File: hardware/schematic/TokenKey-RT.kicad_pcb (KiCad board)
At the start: 4 copper layers, 50 x 40 mm, 103 parts, among them J1 USB-C, J2 Header 1x04 P2.54 H3.0 (OLED), J3 TC2030-NL, Q1 AO3401A, SW1 SW_BOOT, SW2 EC11E18244A5, SW3 BTN1, SW4 BTN2, U1 MIMXRT1062DVL6B, U2 AP2112K-3.3TRG1, U3 TLV62569DBVR, U4 W25Q64JVSSIQ, U5 APS6404L-3SQR-ZR, U6 USBLC6-2SC6, Y1 24MHz 12pF, Y2 32.768kHz 12.5pF

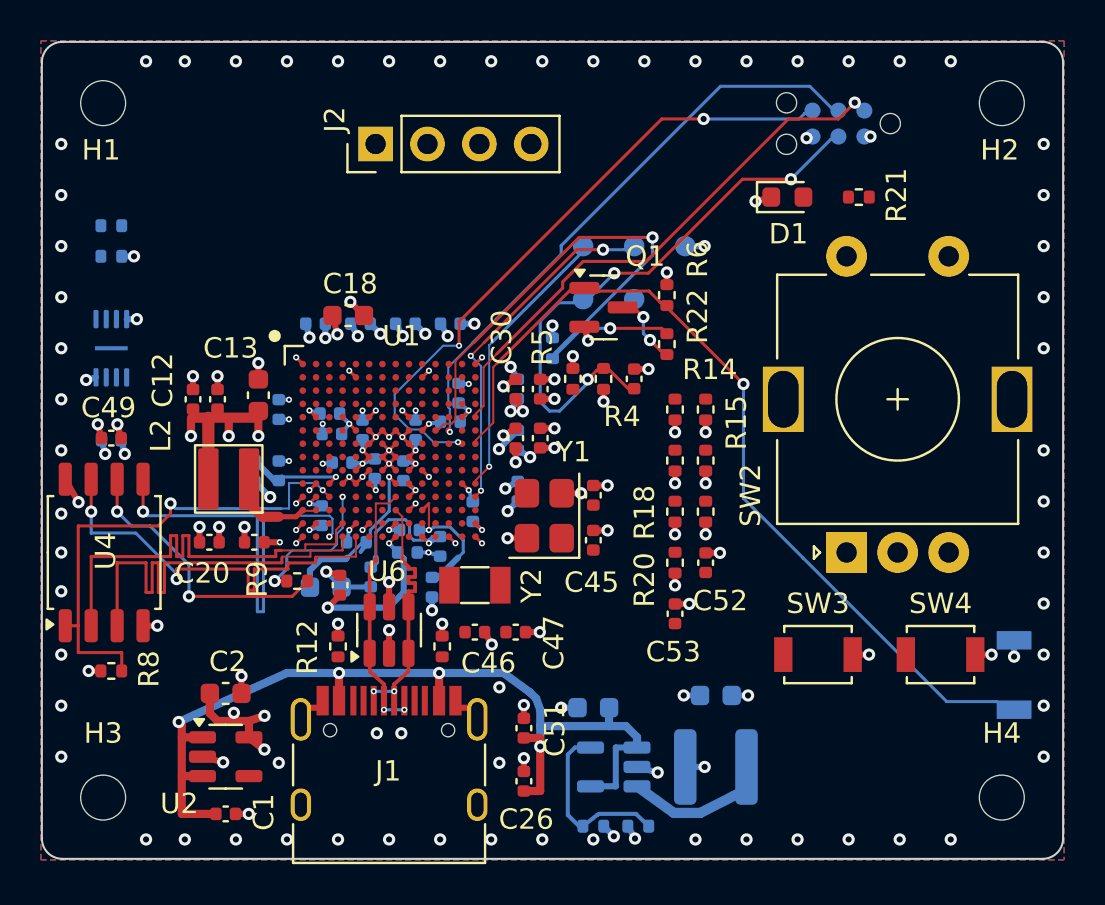
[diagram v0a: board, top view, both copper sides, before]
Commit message: Group B non-U1 legs: R14/R15-J2, D1-R21, R16-C52-SW2, C53-R17-SW2, R18-SW2, R19-SW3, R20-SW4
Part of #60
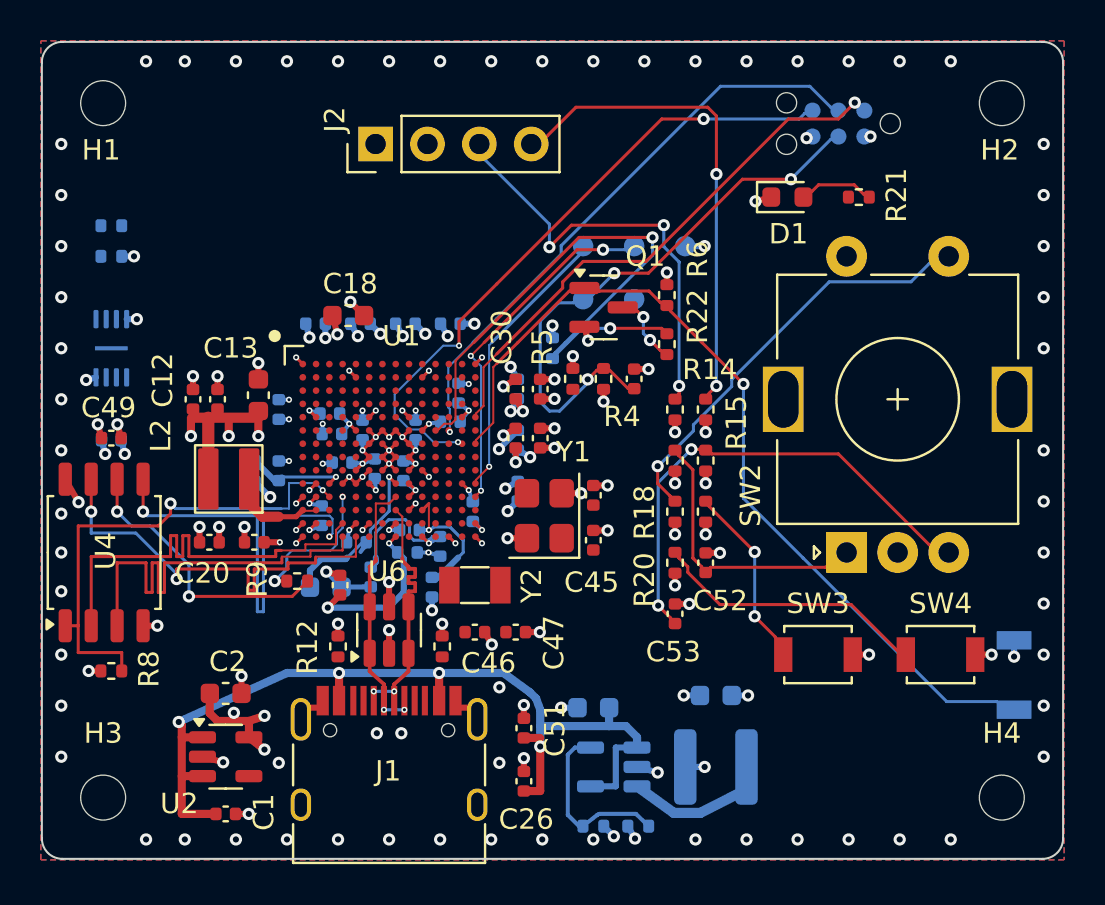
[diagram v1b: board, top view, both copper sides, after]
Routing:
- net ENC_B: track 0.00 -> 24.1 mm, vias 0 -> 2
- net OLED_SDA: track 0.00 -> 24.0 mm, vias 0 -> 2
- net OLED_SCL: track 0.00 -> 21.3 mm, vias 0 -> 3
- net ENC_SW: track 0.00 -> 20.9 mm, vias 0 -> 1
- net ENC_A: track 0.00 -> 13.8 mm
- net BTN2: track 0.00 -> 13.5 mm
- net BTN1: track 0.00 -> 8.99 mm, vias 0 -> 2
- net LED_A: track 0.00 -> 3.66 mm

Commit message: Route CC2 (J1 B5-R13) and 24 MHz XTALI/XTALO U1-Y1, Y1-C44 (no vias; guard ring pending)
Part of #60
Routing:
- net XTALI: track 0.00 -> 9.21 mm
- net XTALO: track 0.00 -> 6.26 mm
- net CC2: track 0.00 -> 2.60 mm
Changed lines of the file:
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@@
 	)
 	(segment
+		(start 18.825 30.625)
+		(end 19.275 30.175)
+		(width 0.15)
+		(layer "F.Cu")
+		(net 3)
+	)
+	(segment
+		(start 18.75 32.255)
+		(end 18.825 31.525)
+		(width 0.15)
+		(layer "F.Cu")
+		(net 3)
+	)
+	(segment
+		(start 19.275 30.175)
+		(end 19.6 30.11)
+		(width 0.15)
+		(layer "F.Cu")
+		(net 3)
+	)
+	(segment
+		(start 18.825 31.525)
+		(end 18.825 30.625)
+		(width 0.15)
+		(layer "F.Cu")
+		(net 3)
+	)
+	(segment
 		(start 30.775 13.175)
 		(end 32.325 14.725)
@@
 	)
 	(segment
+		(start 22.275 25.275)
+		(end 24.3 25.275)
+		(width 0.15)
+		(layer "F.Cu")
+		(net 16)
+	)
+	(segment
+		(start 25.975 23.65)
+		(end 26.725 22.9)
+		(width 0.15)
+		(layer "F.Cu")
+		(net 16)
+	)
+	(segment
+		(start 20.45 25.275)
+		(end 22.275 25.275)
+		(width 0.1)
+		(layer "F.Cu")
+		(net 16)
+	)
+	(segment
+		(start 24.3 25.275)
+		(end 24.85 24.725)
+		(width 0.15)
+		(layer "F.Cu")
+		(net 16)
+	)
+	(segment
+		(start 19.425 24.25)
+		(end 20.45 25.275)
+		(width 0.1)
+		(layer "F.Cu")
+		(net 16)
+	)
+	(segment
+		(start 26.725 22.9)
+		(end 27 22.68)
+		(width 0.15)
+		(layer "F.Cu")
+		(net 16)
+	)
+	(segment
+		(start 25.45 24.3)
+		(end 25.975 23.65)
+		(width 0.15)
+		(layer "F.Cu")
+		(net 16)
+	)
+	(segment
+		(start 24.85 24.725)
+		(end 25.45 24.3)
+		(width 0.15)
+		(layer "F.Cu")
+		(net 16)
+	)
+	(segment
+		(start 19.275 24.225)
+		(end 19.425 24.25)
+		(width 0.1)
+		(layer "F.Cu")
+		(net 16)
+	)
+	(segment
 		(start 18.625 24.225)
 		(end 18.95 24.55)
@@
 	)
 	(segment
+		(start 21.35 23.25)
+		(end 22.2 22.4)
+		(width 0.1)
+		(layer "F.Cu")
+		(net 39)
+	)
+	(segment
+		(start 22.9 21.275)
+		(end 23.175 21.55)
+		(width 0.15)
+		(layer "F.Cu")
+		(net 39)
+	)
+	(segment
+		(start 19.425 23.525)
+		(end 19.7 23.25)
+		(width 0.1)
+		(layer "F.Cu")
+		(net 39)
+	)
+	(segment
+		(start 22.2 22.4)
+		(end 22.2 21.525)
+		(width 0.1)
+		(layer "F.Cu")
+		(net 39)
+	)
+	(segment
+		(start 23.175 21.55)
+		(end 23.75 22.1)
+		(width 0.15)
+		(layer "F.Cu")
+		(net 39)
+	)
+	(segment
+		(start 22.275 21.45)
+		(end 22.45 21.275)
+		(width 0.15)
+		(layer "F.Cu")
+		(net 39)
+	)
+	(segment
+		(start 22.2 21.525)
+		(end 22.275 21.45)
+		(width 0.1)
+		(layer "F.Cu")
+		(net 39)
+	)
+	(segment
+		(start 19.275 23.575)
+		(end 19.425 23.525)
+		(width 0.1)
+		(layer "F.Cu")
+		(net 39)
+	)
+	(segment
+		(start 19.7 23.25)
+		(end 21.35 23.25)
+		(width 0.1)
+		(layer "F.Cu")
+		(net 39)
+	)
+	(segment
+		(start 22.45 21.275)
+		(end 22.9 21.275)
+		(width 0.15)
+		(layer "F.Cu")
+		(net 39)
+	)
+	(segment

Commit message: Route CC1 (J1 A5-R12) with J1 pad-pitch-limited breakout DRU exception (CC1 in J1 courtyard, 0.15 mm)
Part of #60
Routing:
- net CC1: track 0.00 -> 2.76 mm
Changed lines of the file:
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@@
+	)
+	(segment
+		(start 15.75 31.2)
+		(end 14.66 30.11)
+		(width 0.15)
+		(layer "F.Cu")
+		(net 41)
+	)
+	(segment
+		(start 14.66 30.11)
+		(end 14.5 30.11)
+		(width 0.15)
+		(layer "F.Cu")
+		(net 41)
+	)
+	(segment
+		(start 15.75 32.255)
+		(end 15.75 31.2)
+		(width 0.15)
+		(layer "F.Cu")
+		(net 41)
 	)
 	(segment
